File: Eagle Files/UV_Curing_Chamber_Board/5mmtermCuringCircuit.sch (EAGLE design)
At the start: 26 parts, among them IC1 7805T, IC2 L293D, T1 RFP30N06LE, T2 RFP30N06LE

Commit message: started cleaning up board sch and deleted old rev of board
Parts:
- removed MOTOR_A, MOTOR_B: (no value), SparkFun-Connectors:CONN_025MM
- added MOTOR_BREAKOUT: (no value), con-lstb:MA04-1
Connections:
- net N$14: now also MOTOR_BREAKOUT.4; no longer MOTOR_A.2
- net N$15: now also MOTOR_BREAKOUT.3; no longer MOTOR_A.1
- net N$27: now also MOTOR_BREAKOUT.1; no longer MOTOR_B.1
- net N$28: now also MOTOR_BREAKOUT.2; no longer MOTOR_B.2
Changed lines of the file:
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@@
 <?xml version="1.0" encoding="utf-8"?>
 <!DOCTYPE eagle SYSTEM "eagle.dtd">
-<eagle version="9.4.1">
+<eagle version="9.4.0">
 <drawing>
 <settings>
@@
 <part name="GND7" library="supply1" library_urn="urn:adsk.eagle:library:371" deviceset="GND" device=""/>
 <part name="GND10" library="supply1" library_urn="urn:adsk.eagle:library:371" deviceset="GND" device=""/>
-<part name="MOTOR_A" library="SparkFun-Connectors" library_urn="urn:adsk.eagle:library:513" deviceset="CONN_02" device="5MM" package3d_urn="urn:adsk.eagle:package:38044/1"/>
 <part name="ROTARY_ENC" library="SparkFun-Connectors" library_urn="urn:adsk.eagle:library:513" deviceset="CONN_05" device="" package3d_urn="urn:adsk.eagle:package:38104/1"/>
 <part name="GND11" library="supply1" library_urn="urn:adsk.eagle:library:371" deviceset="GND" device=""/>
@@
 <part name="R4" library="rcl" library_urn="urn:adsk.eagle:library:334" deviceset="R-US_" device="R0805" package3d_urn="urn:adsk.eagle:package:23553/2" value="220"/>
 <part name="RELAY_B" library="SparkFun-Connectors" library_urn="urn:adsk.eagle:library:513" deviceset="CONN_02" device="5MM" package3d_urn="urn:adsk.eagle:package:38044/1"/>
-<part name="MOTOR_B" library="SparkFun-Connectors" library_urn="urn:adsk.eagle:library:513" deviceset="CONN_02" device="5MM" package3d_urn="urn:adsk.eagle:package:38044/1"/>
 <part name="IC2" library="st-microelectronics" library_urn="urn:adsk.eagle:library:368" deviceset="L293D" device="" package3d_urn="urn:adsk.eagle:package:26820/1"/>
 <part name="U$1" library="ESP32-DEVKITC" deviceset="ESP32DEVKITC" device=""/>
+<part name="MOTOR_BREAKOUT" library="con-lstb" library_urn="urn:adsk.eagle:library:162" deviceset="MA04-1" device="" package3d_urn="urn:adsk.eagle:package:8337/1"/>
 </parts>
 <sheets>
@@
 <attribute name="VALUE" x="284.48" y="63.5" size="1.778" layer="96"/>
 </instance>
-<instance part="GND7" gate="1" x="218.44" y="5.08" smashed="yes">
-<attribute name="VALUE" x="215.9" y="2.54" size="1.778" layer="96"/>
-</instance>
-<instance part="GND10" gate="1" x="269.24" y="5.08" smashed="yes">
-<attribute name="VALUE" x="266.7" y="2.54" size="1.778" layer="96"/>
-</instance>
-<instance part="MOTOR_A" gate="G$1" x="200.66" y="35.56" smashed="yes">
-<attribute name="VALUE" x="198.12" y="30.734" size="1.778" layer="96" font="vector"/>
-<attribute name="NAME" x="198.12" y="41.148" size="1.778" layer="95" font="vector"/>
+<instance part="GND7" gate="1" x="226.06" y="5.08" smashed="yes">
+<attribute name="VALUE" x="223.52" y="2.54" size="1.778" layer="96"/>
+</instance>
+<instance part="GND10" gate="1" x="261.62" y="5.08" smashed="yes">
+<attribute name="VALUE" x="259.08" y="2.54" size="1.778" layer="96"/>
 </instance>
 <instance part="ROTARY_ENC" gate="G$1" x="160.02" y="106.68" smashed="yes">
@@
 <attribute name="VALUE" x="353.06" y="60.96" size="1.778" layer="96"/>
 </instance>
-<instance part="GND13" gate="1" x="223.52" y="63.5" smashed="yes">
-<attribute name="VALUE" x="220.98" y="60.96" size="1.778" layer="96"/>
+<instance part="GND13" gate="1" x="223.52" y="68.58" smashed="yes">
+<attribute name="VALUE" x="220.98" y="66.04" size="1.778" layer="96"/>
 </instance>
 <instance part="SPEAKER" gate="G$1" x="185.42" y="96.52" smashed="yes">
@@
 <attribute name="NAME" x="147.32" y="38.608" size="1.778" layer="95" font="vector"/>
 </instance>
-<instance part="MOTOR_B" gate="G$1" x="292.1" y="38.1" smashed="yes" rot="R180">
-<attribute name="VALUE" x="294.64" y="42.926" size="1.778" layer="96" font="vector" rot="R180"/>
-<attribute name="NAME" x="294.64" y="32.512" size="1.778" layer="95" font="vector" rot="R180"/>
-</instance>
 <instance part="IC2" gate="G$1" x="243.84" y="35.56" smashed="yes">
 <attribute name="NAME" x="233.68" y="56.896" size="1.778" layer="95"/>
@@
 <instance part="U$1" gate="G$1" x="243.84" y="96.52" smashed="yes" rot="R270">
 <attribute name="NAME" x="248.92" y="123.19" size="1.27" layer="95"/>
+</instance>
+<instance part="MOTOR_BREAKOUT" gate="1" x="314.96" y="50.8" smashed="yes" rot="R270">
+<attribute name="VALUE" x="304.8" y="52.07" size="1.778" layer="96" rot="R270"/>
+<attribute name="NAME" x="320.802" y="52.07" size="1.778" layer="95" rot="R270"/>
 </instance>
 </instances>
@@
 </segment>
 <segment>
-<wire x1="228.6" y1="38.1" x2="218.44" y2="38.1" width="0.1524" layer="91"/>
+<wire x1="228.6" y1="38.1" x2="226.06" y2="38.1" width="0.1524" layer="91"/>
 <pinref part="GND7" gate="1" pin="GND"/>
-<wire x1="218.44" y1="38.1" x2="218.44" y2="33.02" width="0.1524" layer="91"/>
-<wire x1="218.44" y1="33.02" x2="218.44" y2="7.62" width="0.1524" layer="91"/>
-<wire x1="228.6" y1="33.02" x2="218.44" y2="33.02" width="0.1524" layer="91"/>
-<junction x="218.44" y="33.02"/>
+<wire x1="226.06" y1="38.1" x2="226.06" y2="33.02" width="0.1524" layer="91"/>
+<wire x1="226.06" y1="33.02" x2="226.06" y2="7.62" width="0.1524" layer="91"/>
+<wire x1="228.6" y1="33.02" x2="226.06" y2="33.02" width="0.1524" layer="91"/>
+<junction x="226.06" y="33.02"/>
 <pinref part="IC2" gate="G$1" pin="GND1"/>
 <pinref part="IC2" gate="G$1" pin="GND2"/>
 </segment>
 <segment>
-<wire x1="259.08" y1="38.1" x2="269.24" y2="38.1" width="0.1524" layer="91"/>
+<wire x1="259.08" y1="38.1" x2="261.62" y2="38.1" width="0.1524" layer="91"/>
 <pinref part="GND10" gate="1" pin="GND"/>
-<wire x1="269.24" y1="38.1" x2="269.24" y2="33.02" width="0.1524" layer="91"/>
-<wire x1="269.24" y1="33.02" x2="269.24" y2="7.62" width="0.1524" layer="91"/>
-<wire x1="259.08" y1="33.02" x2="269.24" y2="33.02" width="0.1524" layer="91"/>
-<junction x="269.24" y="33.02"/>
+<wire x1="261.62" y1="38.1" x2="261.62" y2="33.02" width="0.1524" layer="91"/>
+<wire x1="261.62" y1="33.02" x2="261.62" y2="7.62" width="0.1524" layer="91"/>
+<wire x1="259.08" y1="33.02" x2="261.62" y2="33.02" width="0.1524" layer="91"/>
+<junction x="261.62" y="33.02"/>
 <pinref part="IC2" gate="G$1" pin="GND3"/>
 <pinref part="IC2" gate="G$1" pin="GND4"/>
@@
 <pinref part="GND13" gate="1" pin="GND"/>
 <wire x1="226.06" y1="86.36" x2="223.52" y2="86.36" width="0.1524" layer="91"/>
-<wire x1="223.52" y1="86.36" x2="223.52" y2="66.04" width="0.1524" layer="91"/>
+<wire x1="223.52" y1="86.36" x2="223.52" y2="71.12" width="0.1524" layer="91"/>
 <pinref part="U$1" gate="G$1" pin="GND@14"/>
 </segment>
@@
 <net name="N$14" class="0">
 <segment>
-<pinref part="MOTOR_A" gate="G$1" pin="2"/>
-<wire x1="208.28" y1="38.1" x2="208.28" y2="43.18" width="0.1524" layer="91"/>
 <wire x1="208.28" y1="43.18" x2="228.6" y2="43.18" width="0.1524" layer="91"/>
 <pinref part="IC2" gate="G$1" pin="1Y"/>
+<wire x1="208.28" y1="43.18" x2="208.28" y2="-2.54" width="0.1524" layer="91"/>
+<pinref part="MOTOR_BREAKOUT" gate="1" pin="4"/>
+<wire x1="208.28" y1="-2.54" x2="317.5" y2="-2.54" width="0.1524" layer="91"/>
+<wire x1="317.5" y1="-2.54" x2="317.5" y2="43.18" width="0.1524" layer="91"/>
 </segment>
 </net>
@@
 <net name="N$15" class="0">
 <segment>
-<pinref part="MOTOR_A" gate="G$1" pin="1"/>
-<wire x1="208.28" y1="35.56" x2="208.28" y2="27.94" width="0.1524" layer="91"/>
-<wire x1="208.28" y1="27.94" x2="228.6" y2="27.94" width="0.1524" layer="91"/>
+<wire x1="213.36" y1="27.94" x2="228.6" y2="27.94" width="0.1524" layer="91"/>
 <pinref part="IC2" gate="G$1" pin="2Y"/>
+<wire x1="213.36" y1="27.94" x2="210.82" y2="0" width="0.1524" layer="91"/>
+<wire x1="210.82" y1="0" x2="314.96" y2="0" width="0.1524" layer="91"/>
+<wire x1="314.96" y1="0" x2="314.96" y2="43.18" width="0.1524" layer="91"/>
+<pinref part="MOTOR_BREAKOUT" gate="1" pin="3"/>
 </segment>
 </net>
@@
 <net name="N$27" class="0">
 <segment>
-<wire x1="259.08" y1="43.18" x2="279.4" y2="43.18" width="0.1524" layer="91"/>
-<pinref part="MOTOR_B" gate="G$1" pin="1"/>
-<wire x1="279.4" y1="43.18" x2="279.4" y2="38.1" width="0.1524" layer="91"/>
-<wire x1="279.4" y1="38.1" x2="284.48" y2="38.1" width="0.1524" layer="91"/>
+<wire x1="259.08" y1="43.18" x2="309.88" y2="43.18" width="0.1524" layer="91"/>
 <pinref part="IC2" gate="G$1" pin="4Y"/>
+<pinref part="MOTOR_BREAKOUT" gate="1" pin="1"/>
 </segment>
 </net>
 <net name="N$28" class="0">
 <segment>
-<wire x1="259.08" y1="27.94" x2="279.4" y2="27.94" width="0.1524" layer="91"/>
-<wire x1="279.4" y1="27.94" x2="279.4" y2="35.56" width="0.1524" layer="91"/>
-<pinref part="MOTOR_B" gate="G$1" pin="2"/>
-<wire x1="279.4" y1="35.56" x2="284.48" y2="35.56" width="0.1524" layer="91"/>
+<wire x1="259.08" y1="27.94" x2="312.42" y2="27.94" width="0.1524" layer="91"/>
+<wire x1="312.42" y1="27.94" x2="312.42" y2="43.18" width="0.1524" layer="91"/>
 <pinref part="IC2" gate="G$1" pin="3Y"/>
-</segment>
-</net>
+<pinref part="MOTOR_BREAKOUT" gate="1" pin="2"/>
+</segment>
+</net>

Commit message: more eagle
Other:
- note added: "Stepper Control"
- moved on the sheet: IC2

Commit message: schematic
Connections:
- removed net N$1: C1.1, C3.+, IC1.VO, IC2.VCC1, R3.2, U$1.5V
- removed net N$30: IC2.3A, U$1.IO14
- removed net N$5 (its old number): R1.2, T2.G, U$1.IO33
- new net N$2: IC2.4A, U$1.IO14
- net N$14: now also C1.1, C3.+, IC1.VO, IC2.VCC1, R1.2, R3.2, T2.G, U$1.5V, U$1.IO33
- net N$29: now also IC2.3A; no longer IC2.4A
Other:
- moved on the sheet: C1, IC2, MOTOR_BREAKOUT

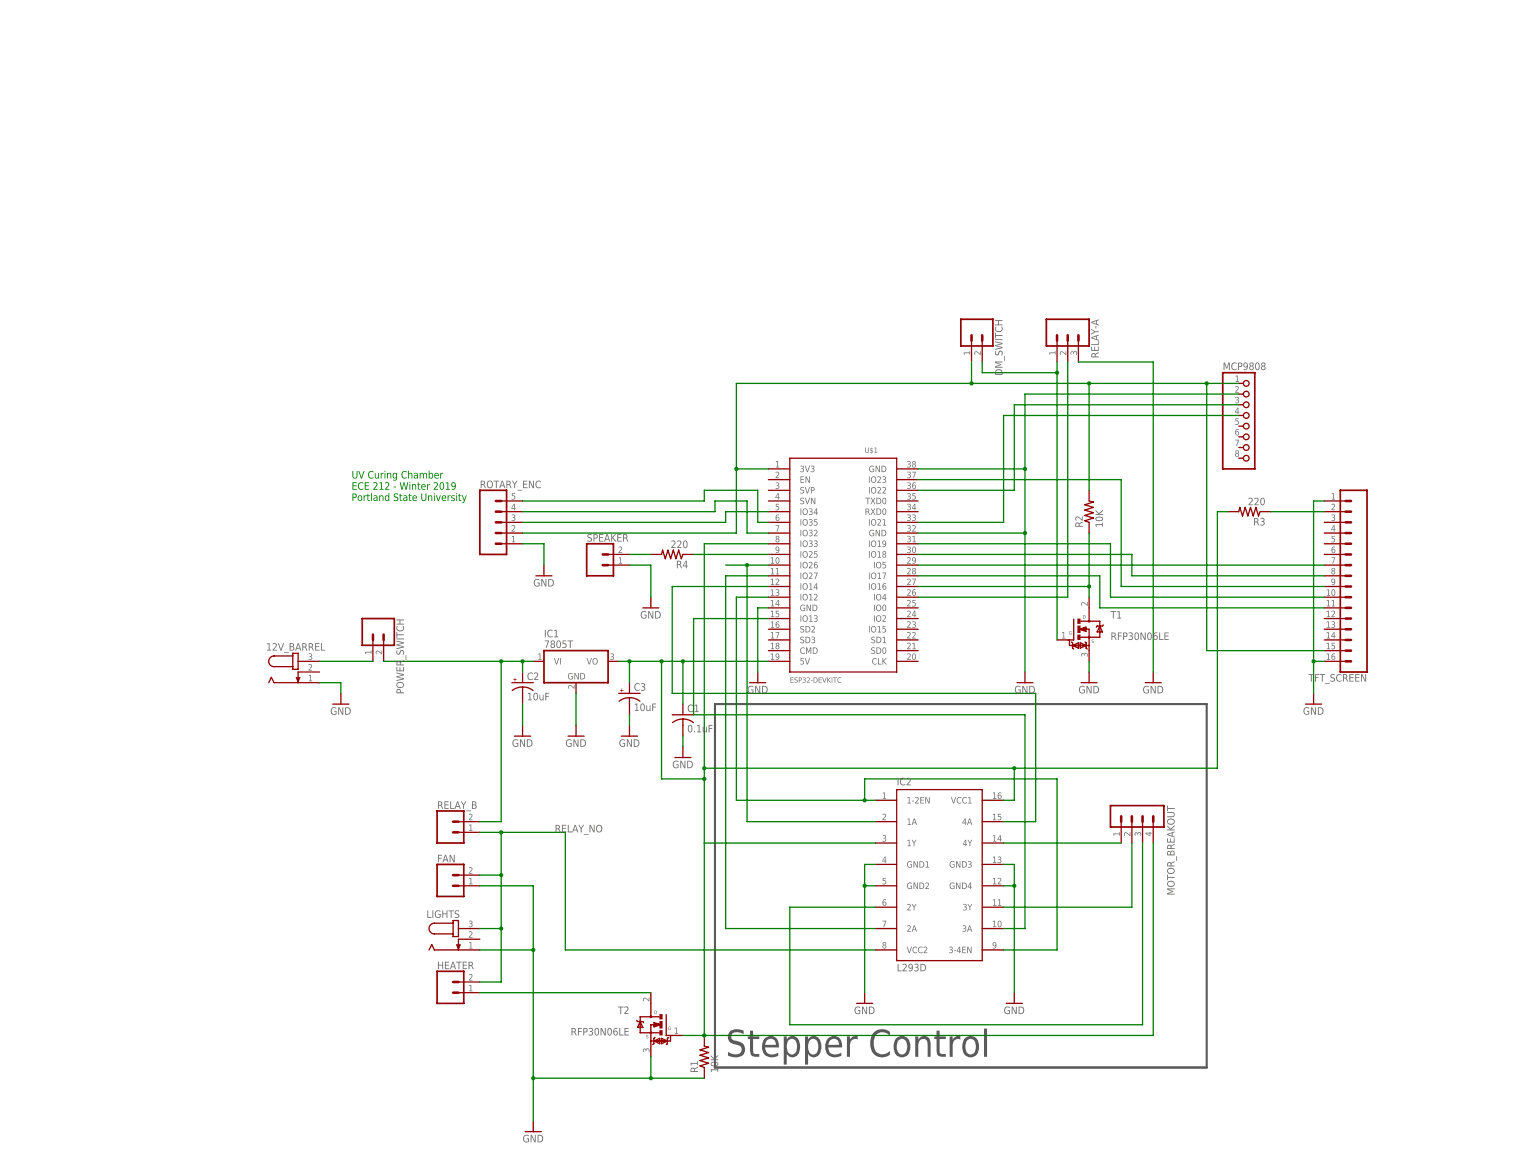
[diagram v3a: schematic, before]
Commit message: removed unnecesary files
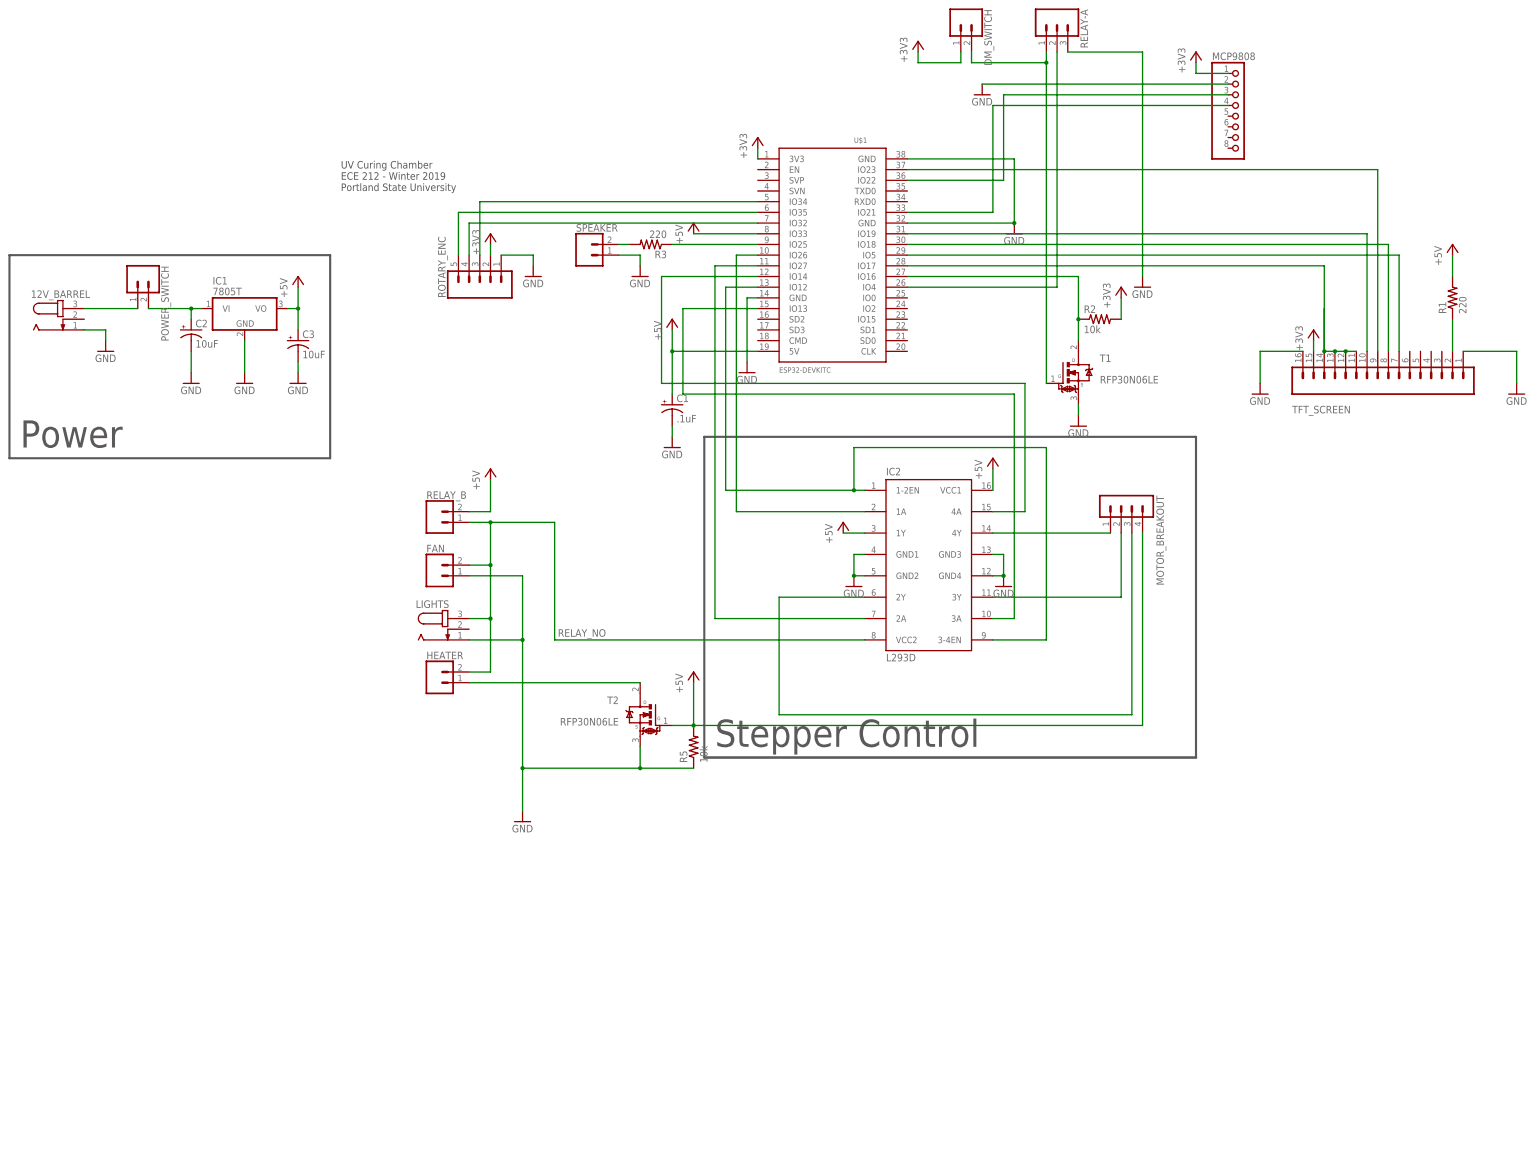
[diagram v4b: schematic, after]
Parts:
- removed R4: 220, rcl:R-US_R0805
- added R5: 10k, rcl:R-US_0207/10
- C1: value 0.1uF -> .1uF; device rcl:C-USC0805 -> rcl:CPOL-USB45181B
- R1: value 10K -> 220; device rcl:R-US_R0805 -> rcl:R-US_0207/10
- R2: value 10K -> 10k; device rcl:R-US_R0805 -> rcl:R-US_0207/10
- R3: device rcl:R-US_R0805 -> rcl:R-US_0207/10
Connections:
- net N$7 renamed +3V3
- removed net N$14: C1.1, C3.+, IC1.VO, IC2.1Y, IC2.VCC1, MOTOR_BREAKOUT.4, R1.2, R3.2, T2.G, U$1.5V, U$1.IO33
- new net +5V: C1.+, C3.+, IC1.VO, IC2.1Y, IC2.VCC1, MOTOR_BREAKOUT.4, R1.2, R5.2, RELAY_B.2, T2.G, U$1.5V, U$1.IO33
- net 12V: no longer RELAY_B.2
- net GND: now also C1.-, R5.1; no longer C1.2, R1.1
- net N$17: now also R1.1; no longer R3.1
- net N$21: now also TFT_SCREEN.12, TFT_SCREEN.13, TFT_SCREEN.14
- net N$26: now also R3.1; no longer R4.1
- net N$6: now also R3.2; no longer R4.2
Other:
- note added: "Power"
- moved on the sheet: 12V_BARREL, C2, C3, DM_SWITCH, FAN, HEATER, IC1, IC2, LIGHTS, MCP9808, MOTOR_BREAKOUT, POWER_SWITCH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

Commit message: more unfucking schematic
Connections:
- net N$21: no longer TFT_SCREEN.12, TFT_SCREEN.13, TFT_SCREEN.14
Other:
- moved on the sheet: C1, MCP9808, R3, SPEAKER, U$1
